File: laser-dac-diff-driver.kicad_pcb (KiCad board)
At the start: 2 copper layers, 52 parts, among them IC401 DCDC-CONV_TRACO_TMH-XXXX_Dual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, P101 CONN_2, P102 CONN_3X2, P103 CONN_6X2, U101 AD5689RARUZ, U102 74HC04, U201 OP470, U202 LM358, U401 LM317EMP, U402 LM317EMP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

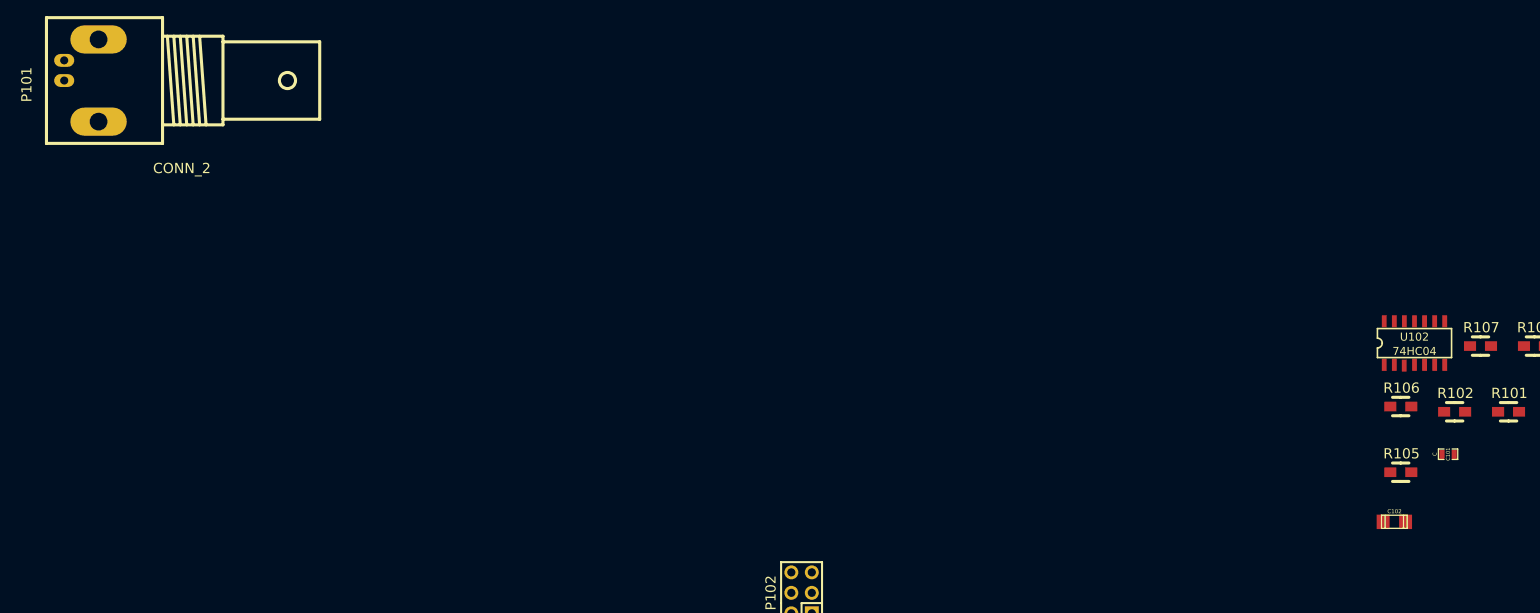
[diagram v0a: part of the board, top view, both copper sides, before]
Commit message: Revert "Moved that thing over there"
This reverts commit 1365cc426dc2828d99ed98a10d059501ce40436a.
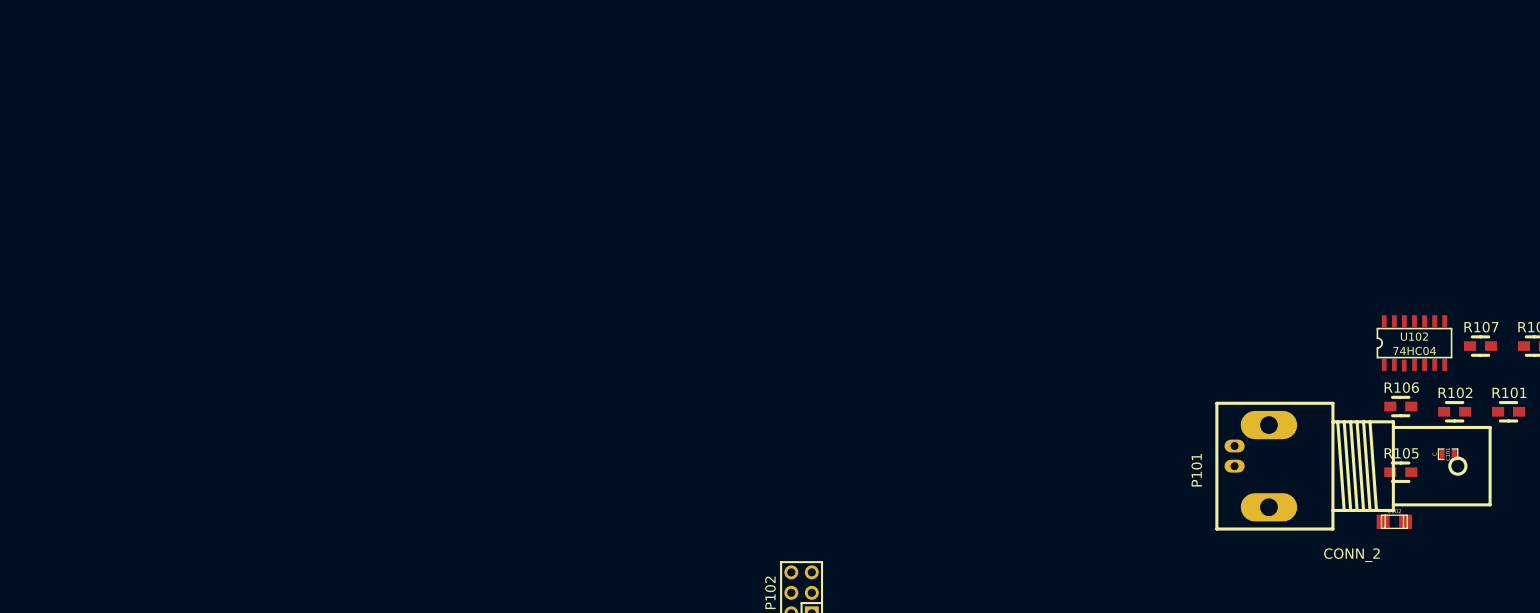
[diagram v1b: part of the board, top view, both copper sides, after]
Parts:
- moved P101 152.9 mm to (182.0, 79.6)
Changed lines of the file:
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@@
-(kicad_pcb (version 3) (host pcbnew "(2014-02-24 BZR 4719)-product")
+(kicad_pcb (version 3) (host pcbnew "(2014-01-30 BZR 4648)-product")
   (general
     (links 128)
     (no_connects 121)
-    (area 97.375133 52.451 288.960587 128.0244)
+    (area 0 0 0 0)
     (thickness 1.6)
     (drawings 0)
@@
     (pad_to_mask_clearance 0.2)
     (aux_axis_origin 0 0)
-    (visible_elements 7FFFFFFF)
+    (visible_elements FFFFFF7F)
     (pcbplotparams
       (layerselection 3178497)
@@
   )
   (module Sockets_BNC:BNC_Socket_TYCO-AMP_LargePads (layer F.Cu)
-    (at 36.83 31.75 270)
+    (at 182.044341 79.595981 270)
     (descr "BNC Socket TYCO AMP")
     (tags "BNC Socket TYCO AMP")

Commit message: Moved that thing over there
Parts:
- moved P101 152.9 mm to (36.8, 31.8)
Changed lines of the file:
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@@
-(kicad_pcb (version 3) (host pcbnew "(2014-01-30 BZR 4648)-product")
+(kicad_pcb (version 3) (host pcbnew "(2014-02-24 BZR 4719)-product")
   (general
     (links 128)
     (no_connects 121)
-    (area 0 0 0 0)
+    (area 97.375133 52.451 288.960587 128.0244)
     (thickness 1.6)
     (drawings 0)
@@
     (pad_to_mask_clearance 0.2)
     (aux_axis_origin 0 0)
-    (visible_elements FFFFFF7F)
+    (visible_elements 7FFFFFFF)
     (pcbplotparams
       (layerselection 3178497)
@@
   )
   (module Sockets_BNC:BNC_Socket_TYCO-AMP_LargePads (layer F.Cu)
-    (at 182.044341 79.595981 270)
+    (at 36.83 31.75 270)
     (descr "BNC Socket TYCO AMP")
     (tags "BNC Socket TYCO AMP")
